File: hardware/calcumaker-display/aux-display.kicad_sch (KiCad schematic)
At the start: 1 part, among them J2 OLED 128x32 (DNP)

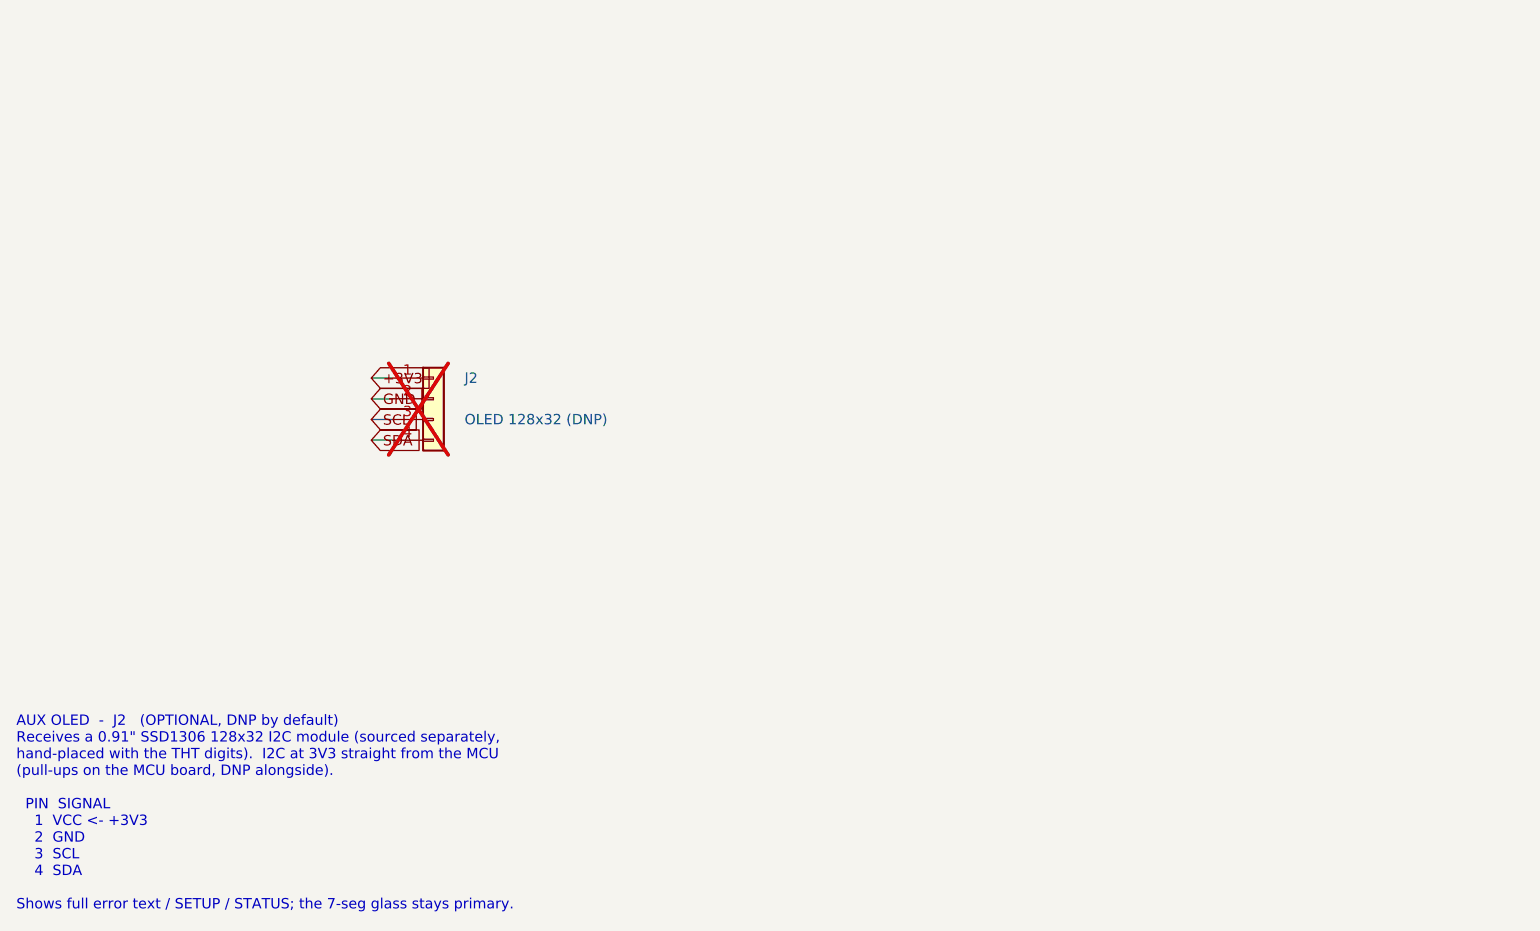
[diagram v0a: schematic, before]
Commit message: Floorplan both display PCBs and verify their schematic nets
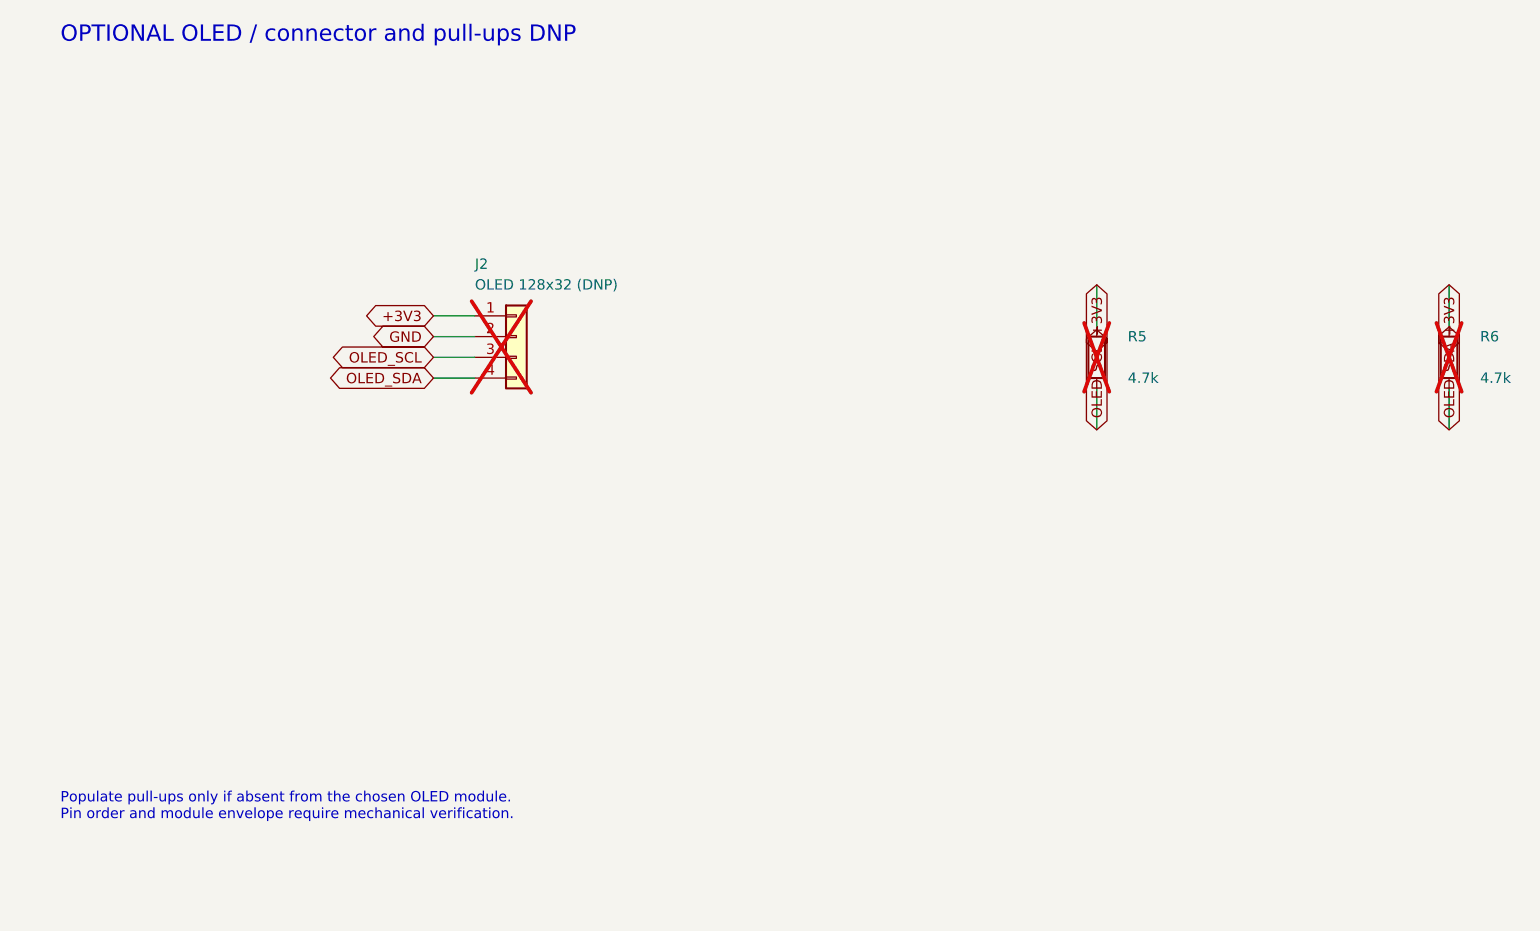
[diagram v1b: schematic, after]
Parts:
- added R5, R6: 4.7k, Resistor_SMD:R_0402_1005Metric, symbol Device:R
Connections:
- net +3V3: now also R5.1, R6.1
- net SCL renamed OLED_SCL
- net OLED_SCL: now also R5.2
- net SDA renamed OLED_SDA
- net OLED_SDA: now also R6.2
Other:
- note added: "OPTIONAL OLED / connector and pull-ups DNP"
- note added: "Populate pull-ups only if absent from the chosen OLED module. Pin order and module envelope require mechanical verification."
- note removed: "AUX OLED - J2 (OPTIONAL, DNP by default) Receives a 0.91" SSD1306 128x32 I2C module (sourced separately, hand-placed with the THT digits). I2C at 3V3 straight from the MCU (pull-ups on the MCU board, DNP alongside). PIN SIGNAL 1 VCC <- +3V3 2 GND 3 SCL 4 SDA Shows full error text / SETUP / STATUS; the 7-seg glass stays primary."
- title: Calcumaker 16 — Display — Aux OLED 128x32 (SSD1306 I2C) — DNP-optional -> Calcumaker 16 / display / aux-display
- moved on the sheet: J2
